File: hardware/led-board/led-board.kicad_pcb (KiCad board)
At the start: 2 copper layers, 178 x 94 mm, 153 parts, among them J1 LINK, J10 PIXEL 4, J11 USB, J2 12V IN, J3 ZONE 1, J4 ZONE 2, J5 ZONE 3, J6 ZONE 4, J7 PIXEL 1, J8 PIXEL 2, J9 PIXEL 3, Q1 BUK9M7R2-40E, Q10 BUK9M7R2-40E, Q11 BUK9M7R2-40E, Q12 BUK9M7R2-40E, Q13 BUK9M7R2-40E, Q14 BUK9M7R2-40E, Q15 BUK9M7R2-40E, Q16 BUK9M7R2-40E, Q17 BSS138, Q18 BSS138, Q2 BUK9M7R2-40E, Q3 BUK9M7R2-40E, Q4 BUK9M7R2-40E, Q5 BUK9M7R2-40E, Q6 BUK9M7R2-40E, Q7 BUK9M7R2-40E, Q8 BUK9M7R2-40E, Q9 BUK9M7R2-40E, SW1 BOOTSEL, SW2 RESET, U1 PCA9615DP, U10 74AHCT1G125, U11 AP2112K-3.3, U2 RP2040, U3 W25Q16JV, U4 INA226, U5 PCA9685PW, U6 AP63205, U7 74AHCT1G125, U8 74AHCT1G125, U9 74AHCT1G125, Y1 12MHz

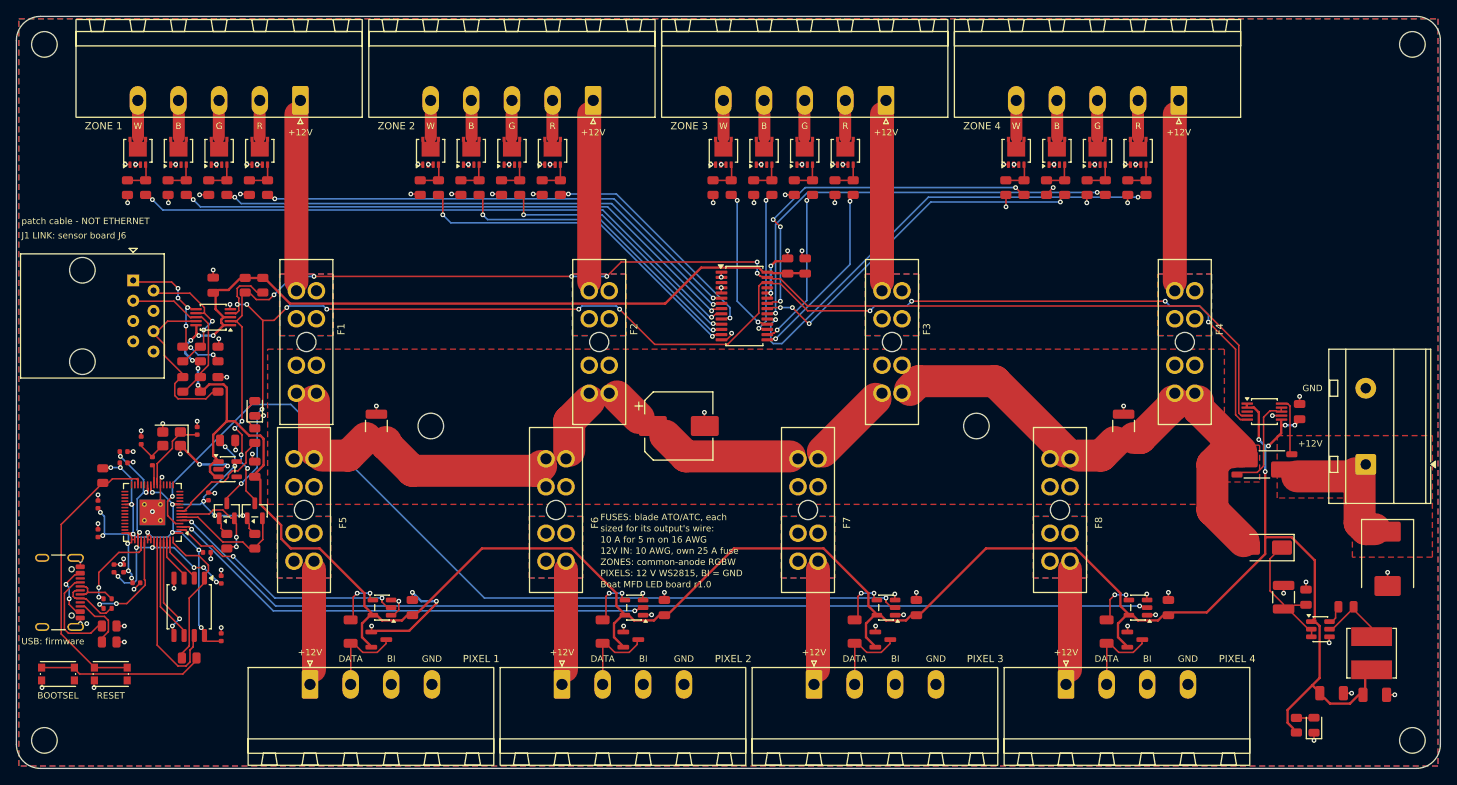
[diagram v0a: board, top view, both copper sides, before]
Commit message: Both boards at 8/8 mil for PCBWay's 2 oz copper
PCBWay only offers 2 oz copper with 8/8 mil minimum track and spacing.

LED board: rerouted at 0.2 mm clearance; ERC, DRC and parity clean.
- Router: no safety margin on straight copper (0.2 mm tracks leave the
  RP2040's 0.4 mm pitch exactly at the limit), a per-curve margin for
  diagonal steps past pad corners, track ends and vias, and no path
  starting from a pad cell too close to its neighbour.
- A bottom-layer ground spoke from the RP2040's exposed pad, laid before
  its supplies close a ring round it.
- The PCA9685's right-hand PWM pins get their vias before SDA/SCL run past.

Sensor board: design rules raised to 0.2 mm; copper unchanged, DRC clean.
Both ORDER.md files say 8/8 mil.

Co-Authored-By: Claude Opus 5.5 <noreply@anthropic.com>
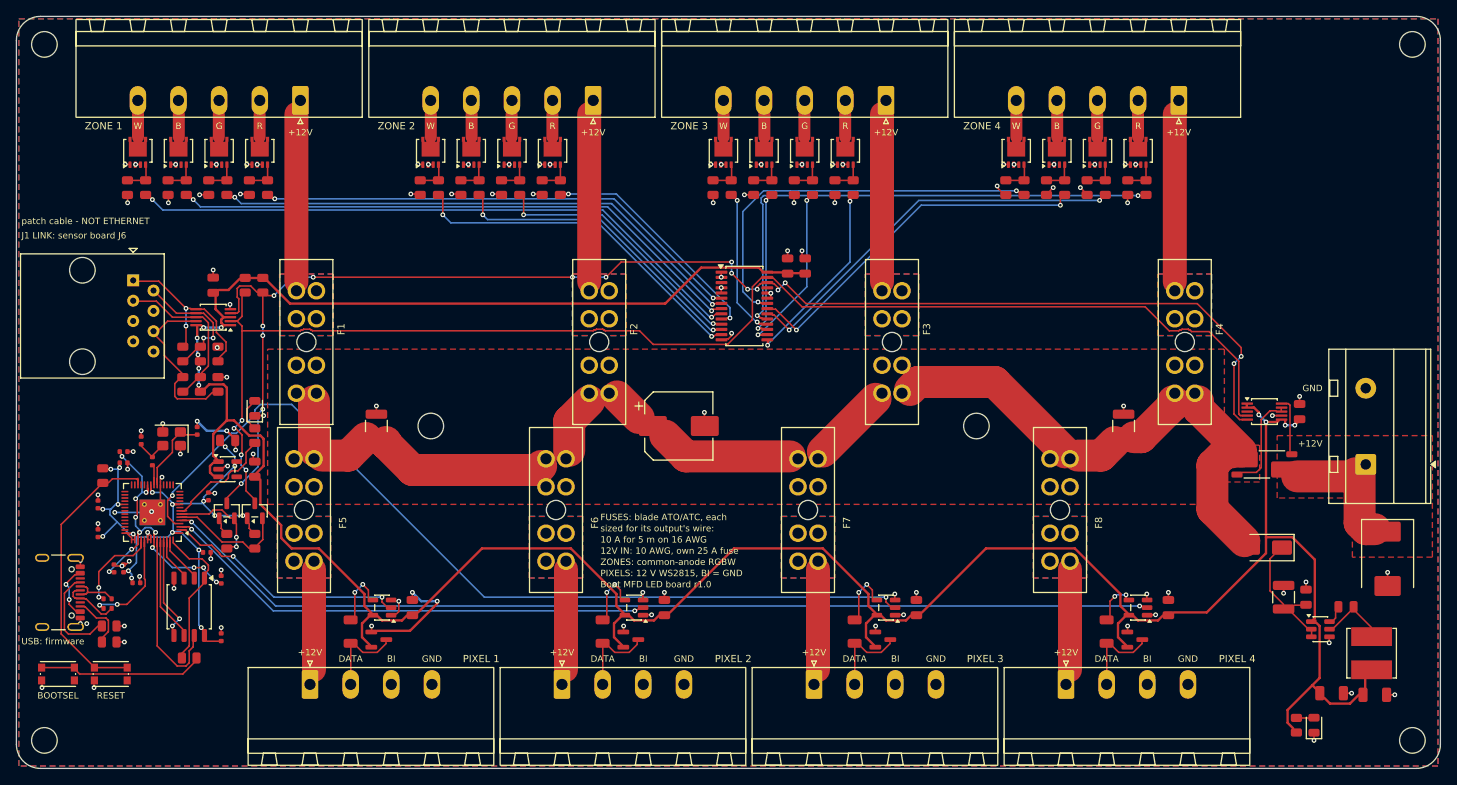
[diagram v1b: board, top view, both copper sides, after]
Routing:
- net /PWM12: track 57.3 -> 64.1 mm
- net +5V: track 348.1 -> 342.7 mm, vias 11 -> 10
- net /PWM15: track 44.3 -> 49.2 mm, vias 4 -> 2
- net /SCL: track 177.4 -> 172.5 mm, vias 12 -> 16
- net /PWM13: track 53.8 -> 48.9 mm
- net +3V3: track 88.1 -> 84.2 mm, vias 20 -> 19
- net /SDA: track 166.0 -> 169.3 mm, vias 10 -> 4
- net /LINK_SCLM: track 17.1 -> 20.2 mm, vias 6 -> 2
- net GND: track 79.3 -> 76.3 mm
- net /PWM9: track 18.8 -> 20.5 mm
- net /PWM8: track 21.8 -> 23.1 mm
- net /LINK_SCLP: track 13.5 -> 12.3 mm
- net /PIX2_5V: track 5.17 -> 6.30 mm
- net /PIX3_5V: track 5.17 -> 6.30 mm
- net /PIX1_5V: track 5.21 -> 6.30 mm
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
